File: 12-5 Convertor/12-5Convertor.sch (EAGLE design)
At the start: 14 parts, among them U1 LM2678

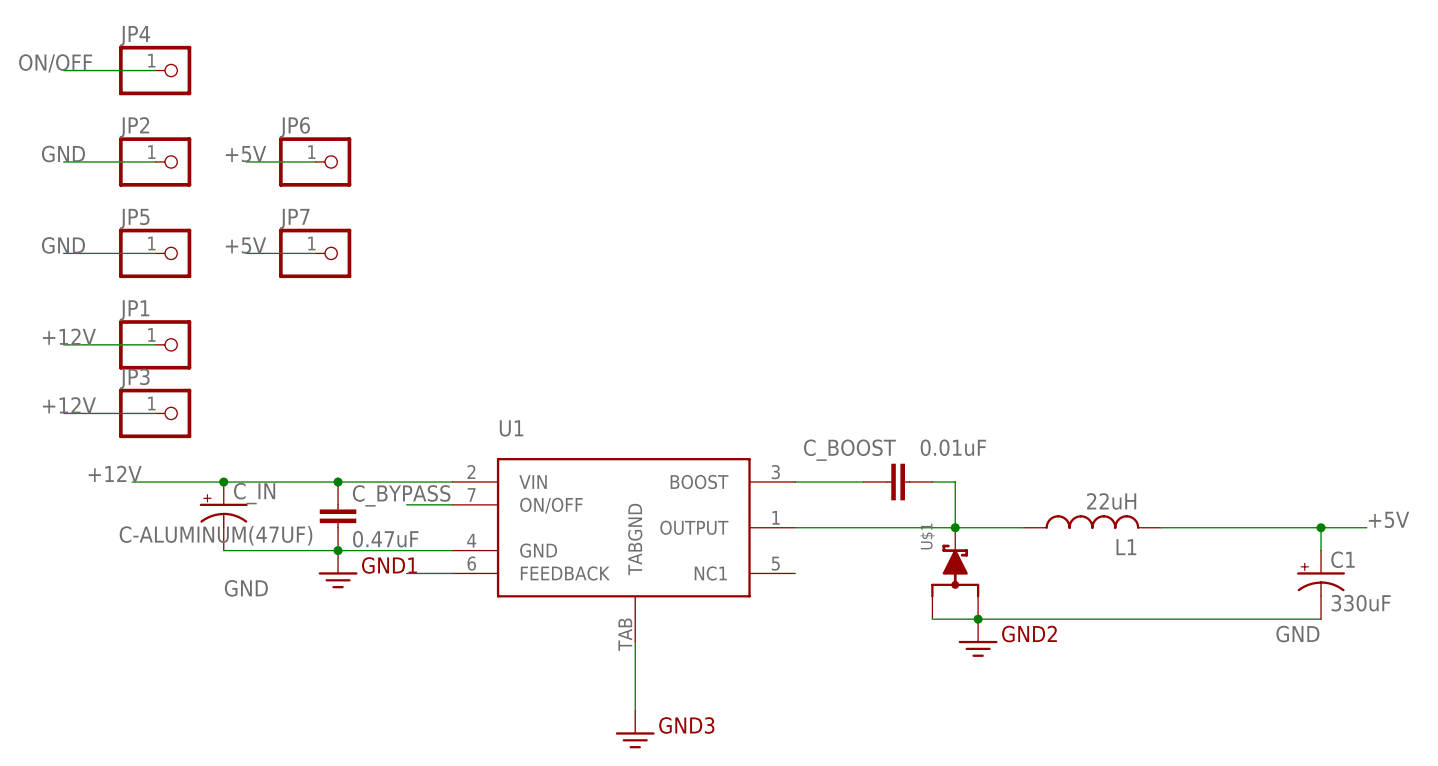
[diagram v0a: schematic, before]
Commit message: Cleaned the 12-5 buck regulator
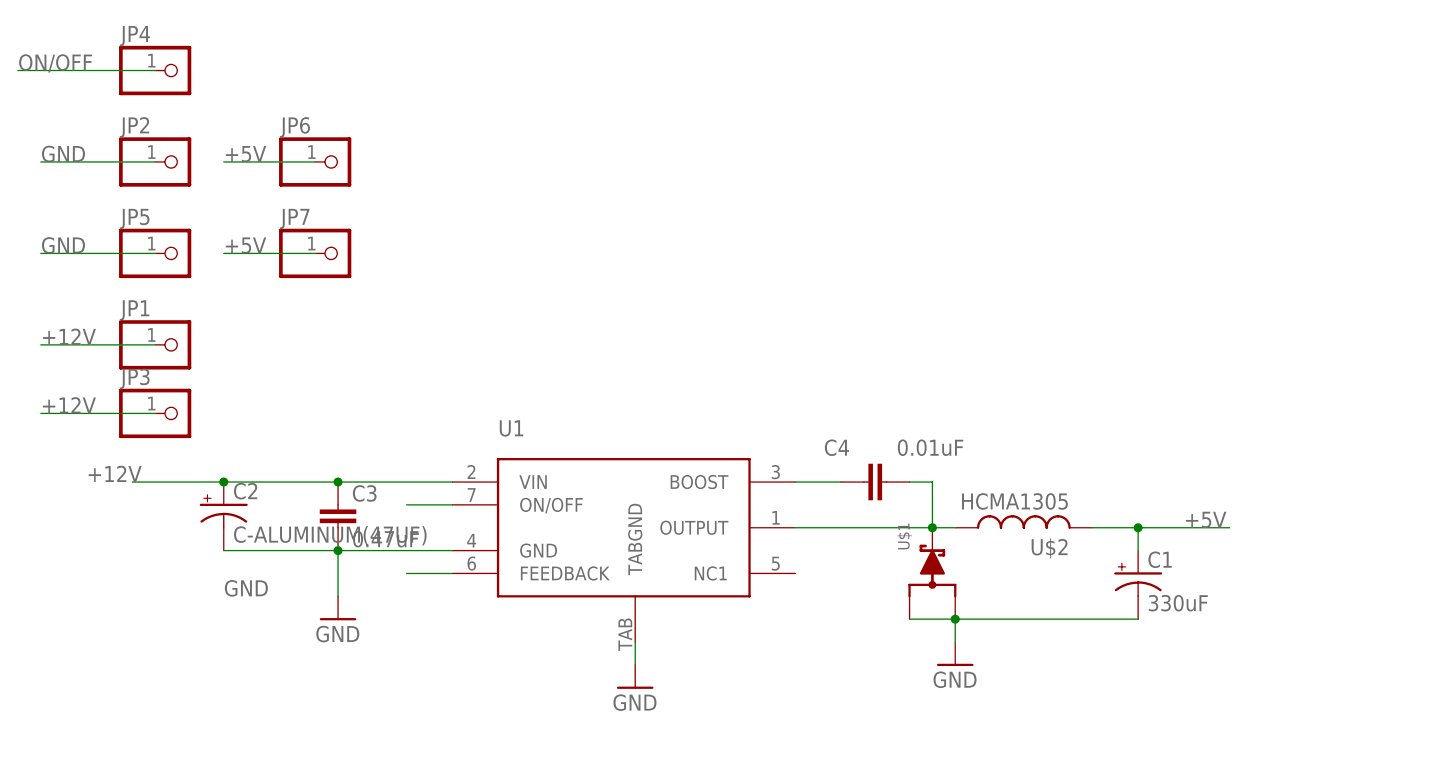
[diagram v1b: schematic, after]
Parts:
- removed C_BOOST: 0.01uF, SparkFun-Passives:CAP0603-CAP
- removed L1: 22uH, DiscreteComponents:SRP1265A
- added C4: 0.01uF, SparkFun-Passives:CAP0603-CAP
- added U$2: HCMA1305, DiscreteComponents:HCMA1305
- renumbered C_BYPASS to C3, C_IN to C2
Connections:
- net +5V: now also U$2.2; no longer L1.2
- net N$2: now also C4.1; no longer C_BOOST.1
- net N$3: now also C4.2, U$2.1; no longer C_BOOST.2, L1.1
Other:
- moved on the sheet: C1, U$1
